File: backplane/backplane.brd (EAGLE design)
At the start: 192 x 80 mm, 16 parts, among them J1 5535070-4, J2 5535070-4, J3 5535070-4, J4 5535070-4, J5 5535070-4, J6 5535070-4, J7 5535070-4, J8 5535070-4, U1 LM1084IS-5.0, U2 LM1084IS-3.3

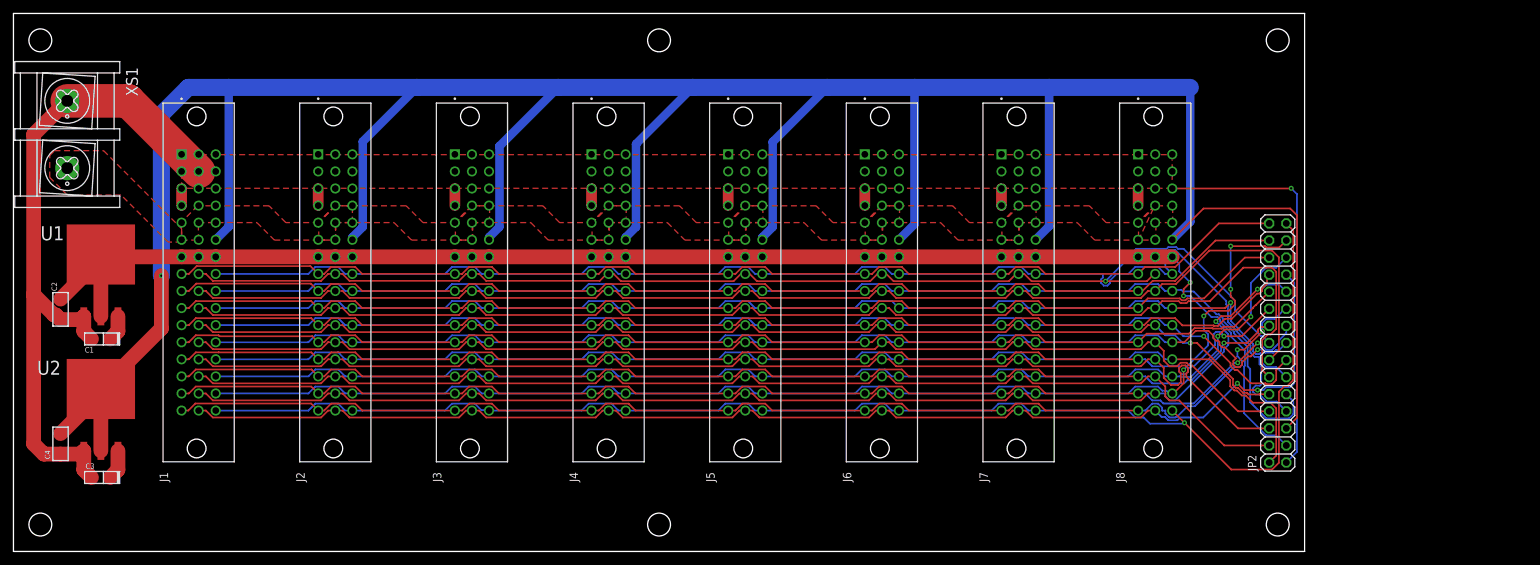
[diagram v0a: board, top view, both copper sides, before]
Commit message: worked on the perfboard prototype card, validated the valves board mechanism
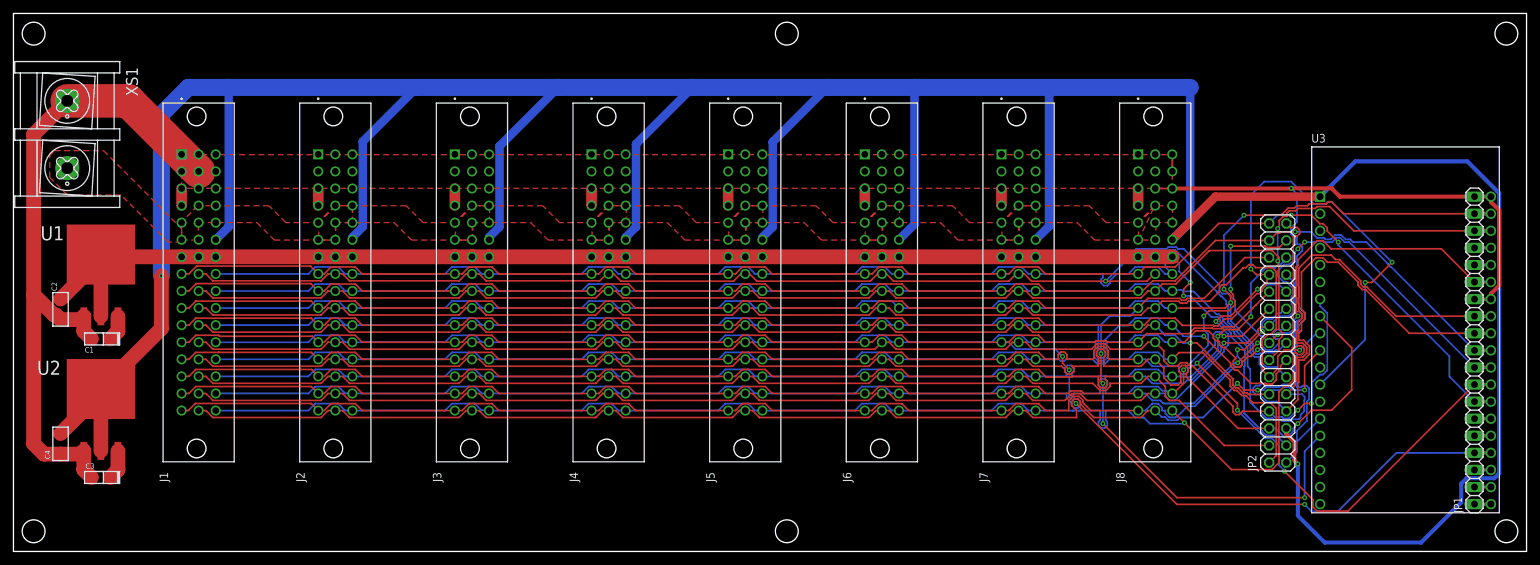
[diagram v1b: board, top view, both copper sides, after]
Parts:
- added JP1: (no value), pinhead:1X19
- added U3: ESP32-DEVKITC-32D, ESP32-DEVKITC-32D:MODULE_ESP32-DEVKITC-32D
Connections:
- new net N$3: JP1.16, U3.23
- new net N$4: JP1.15, U3.24
- new net N$5: JP1.6, U3.33
- new net N$6: JP1.5, U3.34
- new net N$7: JP1.3, U3.36
- new net N$8: JP1.2, U3.37
- new net N$9: JP1.1, U3.38
- new net VCC: U3.19
- net 3.3V: now also U3.1
- net GND: now also JP1.13, JP1.19, U3.14, U3.20, U3.26
- net MISO: now also JP1.12, U3.27
- net MOSI: now also JP1.18, U3.21
- net SCK: now also JP1.11, U3.28
- net SS_1: now also JP1.7, U3.32
- net SS_10: now also U3.9
- net SS_11: now also U3.10
- net SS_12: now also U3.7
- net SS_13: now also U3.8
- net SS_2: now also JP1.10, U3.29
- net SS_3: now also U3.15
- net SS_4: now also U3.12
- net SS_5: now also JP1.4, U3.35
- net SS_6: now also JP1.8, U3.31
- net SS_7: now also JP1.9, U3.30
- net SS_8: now also JP1.14, U3.25
- net SS_9: now also JP1.17, U3.22
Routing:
- net 3.3V: track 474.3 -> 569.4 mm, vias 1 -> 2
- net SS_5: track 170.9 -> 260.8 mm, vias 0 -> 4
- net SS_6: track 175.2 -> 243.4 mm, vias 1 -> 4
- net SS_3: track 171.1 -> 237.2 mm, vias 0 -> 4
- net GND: track 182.5 -> 247.4 mm
- net SS_4: track 172.6 -> 236.9 mm, vias 0 -> 3
- net MISO: track 182.8 -> 242.7 mm
- net SCK: track 190.0 -> 248.3 mm
- net SS_7: track 172.6 -> 230.4 mm, vias 1 -> 3
- net MOSI: track 173.3 -> 226.2 mm, vias 1 -> 3
- net SS_8: track 181.7 -> 229.9 mm, vias 1 -> 3
- net SS_1: track 170.9 -> 218.2 mm, vias 0 -> 2
- net SS_2: track 170.9 -> 212.3 mm, vias 0 -> 1
- net SS_9: track 185.4 -> 226.3 mm, vias 0 -> 2
- net SS_13: track 175.4 -> 211.8 mm, vias 0 -> 1
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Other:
- board size 192 x 80 mm -> 225 x 80 mm

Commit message: added cam data
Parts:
- J1, J2, J3, J4, J5, J6, J7, J8: value 5535070-4 -> 09232486825; device 5535070-4:TE_5535070-4 -> din41612_48_pin_backplane:HARTING_09232486825
- U1, U2: device LM1084IS-5.0:TO254P1435X457-3N -> LM1084IS:TO254P1435X457-3N
